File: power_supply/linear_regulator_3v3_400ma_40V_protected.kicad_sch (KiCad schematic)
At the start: 10 parts

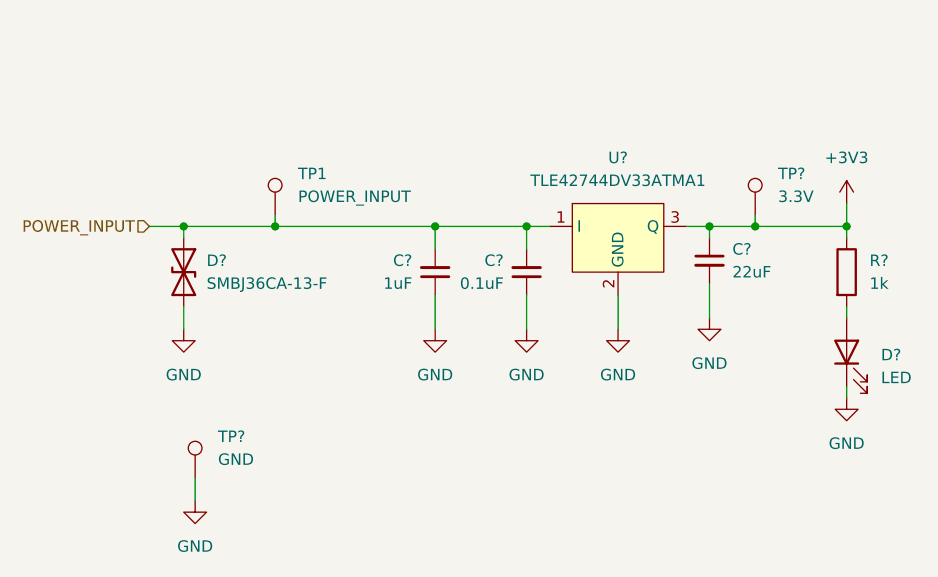
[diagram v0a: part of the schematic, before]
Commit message: Updated README
cleaned up some test points
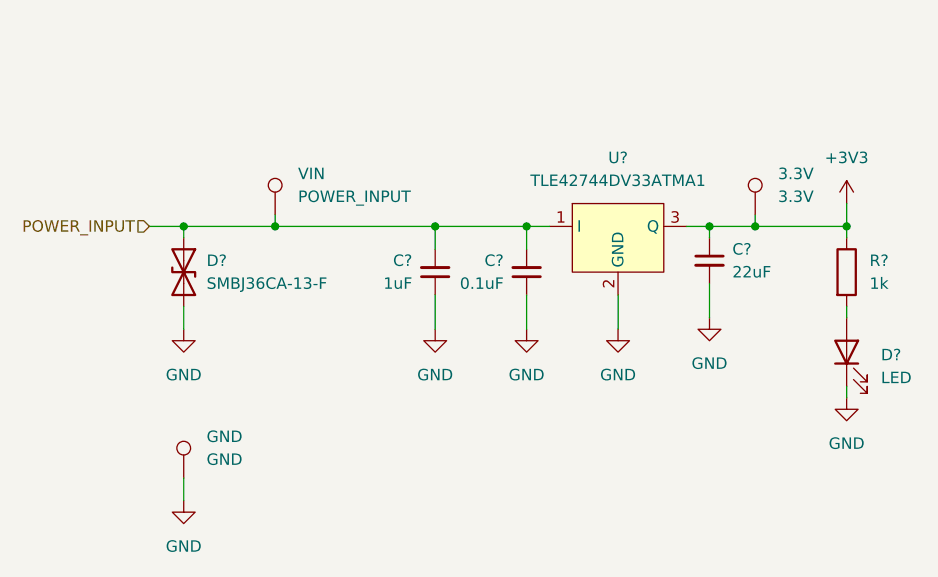
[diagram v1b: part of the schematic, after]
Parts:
- gave numbers to parts that had none: 2
- renumbered TP1 to VIN
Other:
- moved on the sheet: GND
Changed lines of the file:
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@@
 	(wire
 		(pts
-			(xy 116.84 119.38) (xy 116.84 121.92)
+			(xy 115.57 119.38) (xy 115.57 121.92)
 		)
 		(stroke
@@
 	(symbol
 		(lib_id "power:GND")
-		(at 116.84 121.92 0)
+		(at 115.57 121.92 0)
 		(unit 1)
 		(exclude_from_sim no)
@@
 		(fields_autoplaced yes)
 		(property "Reference" "#PWR?"
-			(at 116.84 128.27 0)
+			(at 115.57 128.27 0)
 			(effects
 				(font
@@
 		)
 		(property "Value" "GND"
-			(at 116.84 127 0)
+			(at 115.57 127 0)
 			(effects
 				(font
@@
 		)
 		(property "Footprint" ""
-			(at 116.84 121.92 0)
+			(at 115.57 121.92 0)
 			(effects
 				(font
@@
 		)
 		(property "Datasheet" ""
-			(at 116.84 121.92 0)
-			(effects
-				(font
-					(size 1.27 1.27)
-				)
-				(hide yes)
-			)
-		)
-		(property "Description" ""
-			(at 116.84 121.92 0)
+			(at 115.57 121.92 0)
+			(effects
+				(font
+					(size 1.27 1.27)
+				)
+				(hide yes)
+			)
+		)
+		(property "Description" ""
+			(at 115.57 121.92 0)
 			(effects
 				(font
@@
 		(dnp no)
 		(fields_autoplaced yes)
-		(property "Reference" "TP?"
+		(property "Reference" "3.3V"
 			(at 181.61 85.5979 0)
 			(effects
@@
 			(project "power_supply_3v3_400ma_40V_protected"
 				(path "/49cac681-4fee-4c3c-9188-8849ebd3eabe"
-					(reference "TP?")
+					(reference "3.3V")
 					(unit 1)
 				)
@@
 	(symbol
 		(lib_id "Connector:TestPoint")
-		(at 116.84 119.38 0)
-		(unit 1)
-		(exclude_from_sim no)
-		(in_bom yes)
-		(on_board yes)
-		(dnp no)
-		(fields_autoplaced yes)
-		(property "Reference" "TP?"
-			(at 119.38 114.8079 0)
+		(at 115.57 119.38 0)
+		(unit 1)
+		(exclude_from_sim no)
+		(in_bom yes)
+		(on_board yes)
+		(dnp no)
+		(fields_autoplaced yes)
+		(property "Reference" "GND"
+			(at 118.11 114.8079 0)
 			(effects
 				(font
@@
 		)
 		(property "Value" "GND"
-			(at 119.38 117.3479 0)
+			(at 118.11 117.3479 0)
 			(effects
 				(font
@@
 		)
 		(property "Footprint" "TestPoint:TestPoint_Pad_D2.0mm"
-			(at 121.92 119.38 0)
+			(at 120.65 119.38 0)
 			(effects
 				(font
@@
 		)
 		(property "Datasheet" "~"
-			(at 121.92 119.38 0)
-			(effects
-				(font
-					(size 1.27 1.27)
-				)
-				(hide yes)
-			)
-		)
-		(property "Description" ""
-			(at 116.84 119.38 0)
-			(effects
-				(font
-					(size 1.27 1.27)
-				)
-			)
-		)
-		(pin "1"
-		)
-		(instances
-			(project "power_supply_3v3_400ma_40V_protected"
-				(path "/49cac681-4fee-4c3c-9188-8849ebd3eabe"
-					(reference "TP?")
+			(at 120.65 119.38 0)
+			(effects
+				(font
+					(size 1.27 1.27)
+				)
+				(hide yes)
+			)
+		)
+		(property "Description" ""
+			(at 115.57 119.38 0)
+			(effects
+				(font
+					(size 1.27 1.27)
+				)
+			)
+		)
+		(pin "1"
+		)
+		(instances
+			(project "power_supply_3v3_400ma_40V_protected"
+				(path "/49cac681-4fee-4c3c-9188-8849ebd3eabe"
+					(reference "GND")
 					(unit 1)
 				)
@@
 		(dnp no)
 		(fields_autoplaced yes)
-		(property "Reference" "TP1"
+		(property "Reference" "VIN"
 			(at 128.27 85.5979 0)
 			(effects
@@
 			(project "power_supply_3v3_400ma_40V_protected"
 				(path "/49cac681-4fee-4c3c-9188-8849ebd3eabe"
-					(reference "TP1")
-					(unit 1)
-				)
+					(reference "VIN")
+					(unit 1)
+				)
